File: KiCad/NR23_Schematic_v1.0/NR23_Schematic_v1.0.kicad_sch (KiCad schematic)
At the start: 0 parts

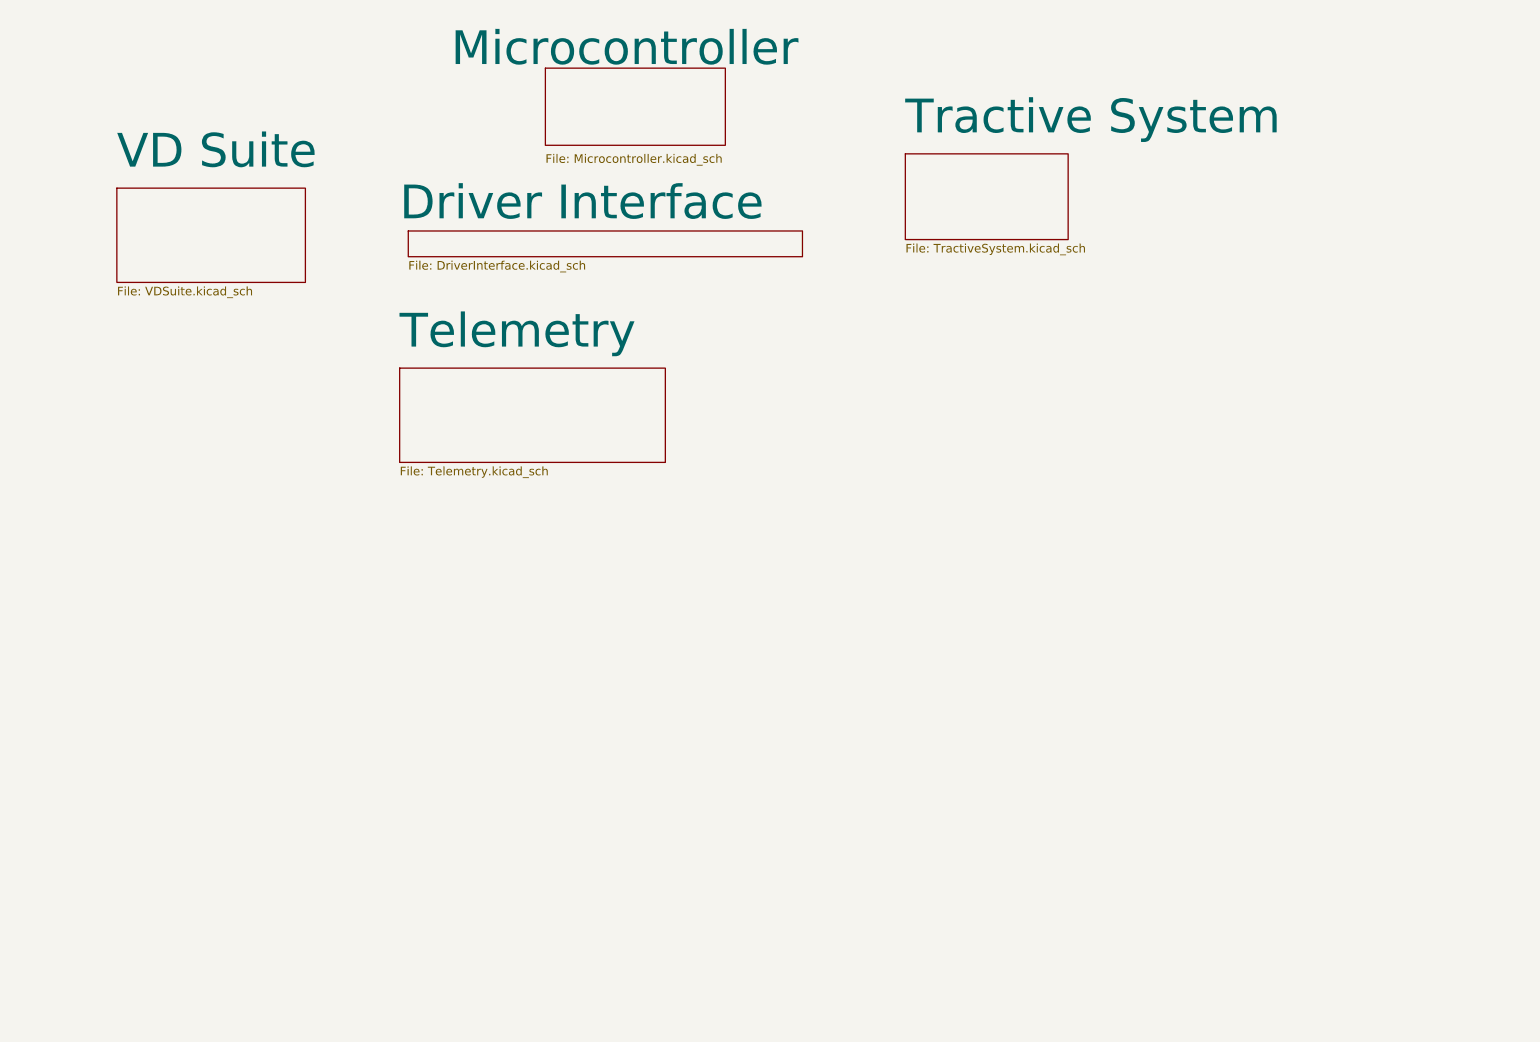
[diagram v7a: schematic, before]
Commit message: fixed throttle wiring
removed throttle resistor and wired throttle pins 2 and 4 together
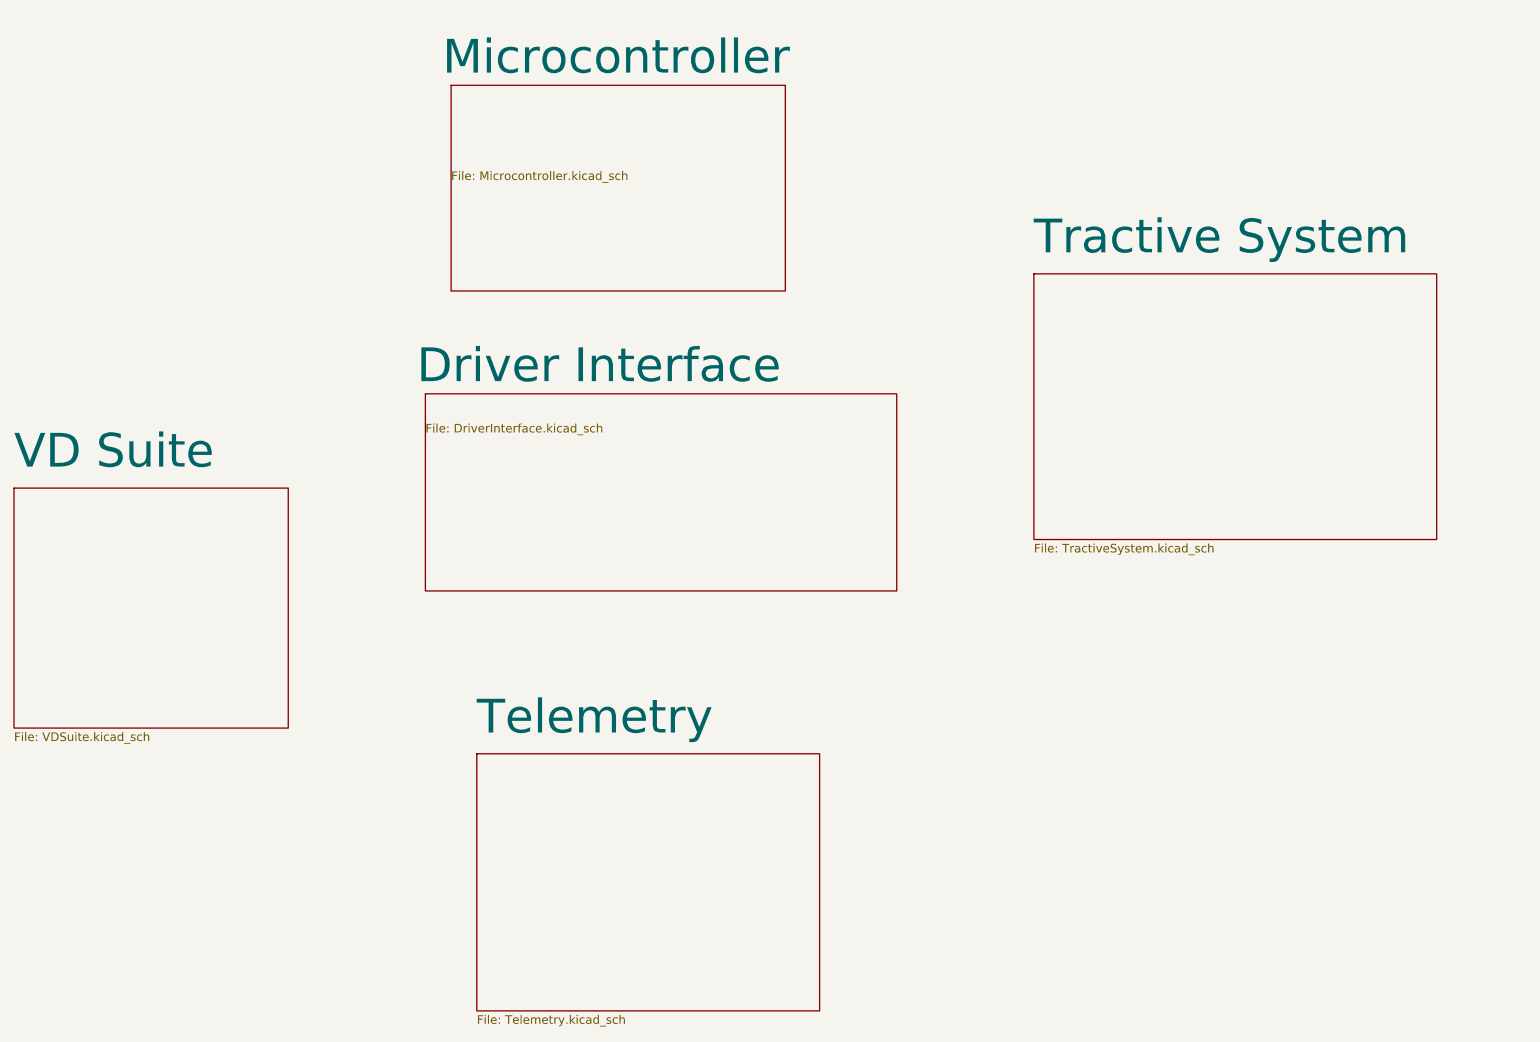
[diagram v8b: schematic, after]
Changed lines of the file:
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@@
 (kicad_sch (version 20211123) (generator eeschema)
   (paper "A")
-  (sheet (at 85.09 78.74) (size 39.37 13.97) (fields_autoplaced)
+  (title_block
+    (date "2023-02-28")
+  )
+  (sheet (at 96.52 135.89) (size 50.8 38.1)
     (stroke (width 0.1524) (type solid) (color 0 0 0 0))
     (fill (color 0 0 0 0.0000))
-    (property "Sheet name" "Telemetry" (id 0) (at 85.09 76.1634 0)
+    (property "Sheet name" "Telemetry" (id 0) (at 96.52 133.35 0)
       (effects (font (size 5 5)) (justify left bottom))
     )
-    (property "Sheet file" "Telemetry.kicad_sch" (id 1) (at 85.09 93.2946 0)
+    (property "Sheet file" "Telemetry.kicad_sch" (id 1) (at 96.52 174.5746 0)
       (effects (font (size 1.27 1.27)) (justify left top))
     )
   )
-  (sheet (at 43.18 52.07) (size 27.94 13.97) (fields_autoplaced)
+  (sheet (at 27.94 96.52) (size 40.64 35.56) (fields_autoplaced)
     (stroke (width 0.1524) (type solid) (color 0 0 0 0))
     (fill (color 0 0 0 0.0000))
-    (property "Sheet name" "VD Suite" (id 0) (at 43.18 49.4934 0)
+    (property "Sheet name" "VD Suite" (id 0) (at 27.94 93.9434 0)
       (effects (font (size 5 5)) (justify left bottom))
     )
-    (property "Sheet file" "VDSuite.kicad_sch" (id 1) (at 43.18 66.6246 0)
+    (property "Sheet file" "VDSuite.kicad_sch" (id 1) (at 27.94 132.6646 0)
       (effects (font (size 1.27 1.27)) (justify left top))
     )
   )
-  (sheet (at 86.36 58.42) (size 58.42 3.81)
+  (sheet (at 88.9 82.55) (size 69.85 29.21)
     (stroke (width 0.1524) (type solid) (color 0 0 0 0))
     (fill (color 0 0 0 0.0000))
-    (property "Sheet name" "Driver Interface" (id 0) (at 85.09 57.15 0)
+    (property "Sheet name" "Driver Interface" (id 0) (at 87.63 81.28 0)
       (effects (font (size 5 5)) (justify left bottom))
     )
-    (property "Sheet file" "DriverInterface.kicad_sch" (id 1) (at 86.36 62.8146 0)
+    (property "Sheet file" "DriverInterface.kicad_sch" (id 1) (at 88.9 86.9446 0)
       (effects (font (size 1.27 1.27)) (justify left top))
     )
   )
-  (sheet (at 160.02 46.99) (size 24.13 12.7) (fields_autoplaced)
+  (sheet (at 179.07 64.77) (size 59.69 39.37) (fields_autoplaced)
     (stroke (width 0.1524) (type solid) (color 0 0 0 0))
     (fill (color 0 0 0 0.0000))
-    (property "Sheet name" "Tractive System" (id 0) (at 160.02 44.4134 0)
+    (property "Sheet name" "Tractive System" (id 0) (at 179.07 62.1934 0)
       (effects (font (size 5 5)) (justify left bottom))
     )
-    (property "Sheet file" "TractiveSystem.kicad_sch" (id 1) (at 160.02 60.2746 0)
+    (property "Sheet file" "TractiveSystem.kicad_sch" (id 1) (at 179.07 104.7246 0)
       (effects (font (size 1.27 1.27)) (justify left top))
     )
   )
-  (sheet (at 106.68 34.29) (size 26.67 11.43)
+  (sheet (at 92.71 36.83) (size 49.53 30.48)
     (stroke (width 0.1524) (type solid) (color 0 0 0 0))
     (fill (color 0 0 0 0.0000))
-    (property "Sheet name" "Microcontroller" (id 0) (at 92.71 34.29 0)
+    (property "Sheet name" "Microcontroller" (id 0) (at 91.44 35.56 0)
       (effects (font (size 5 5)) (justify left bottom))
     )
-    (property "Sheet file" "Microcontroller.kicad_sch" (id 1) (at 106.68 46.99 0)
+    (property "Sheet file" "Microcontroller.kicad_sch" (id 1) (at 92.71 49.53 0)
       (effects (font (size 1.27 1.27)) (justify left top))
     )
@@
       (reference "M1") (unit 1) (value "Zero_7R_Motor") (footprint "")
     )
-    (path "/8302703f-65d0-4b91-aeea-6f721ab57e4c/4b73d085-8847-4f3e-8b8e-a264476cb21e"
-      (reference "R_pullup") (unit 1) (value "10k") (footprint "")
-    )
     (path "/8302703f-65d0-4b91-aeea-6f721ab57e4c/737b7baf-b889-4aeb-8cad-49a9c6801593"
